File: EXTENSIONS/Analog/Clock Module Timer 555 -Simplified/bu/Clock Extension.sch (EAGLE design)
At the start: 8 parts, among them T555_CLOCK NE555N, X1 USB-A

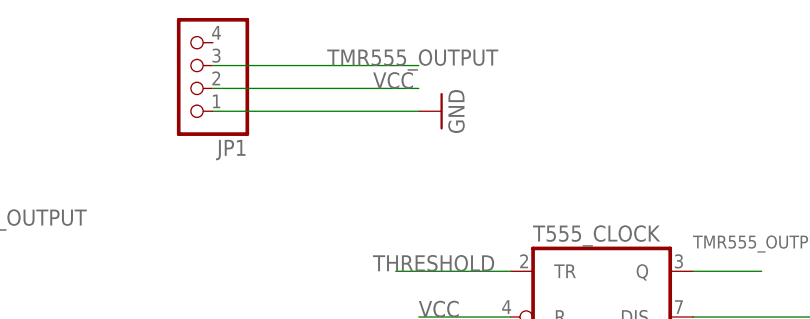
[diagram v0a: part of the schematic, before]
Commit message: fix bug in pcb '0 TO 9 Counter 74LS90'
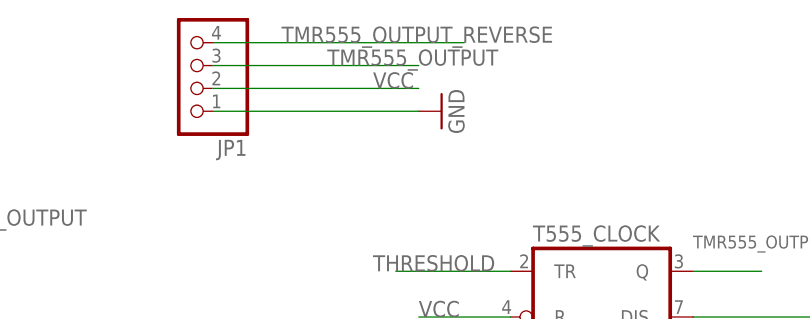
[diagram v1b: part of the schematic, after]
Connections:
- new net TMR555_OUTPUT_REVERSE: JP1.4
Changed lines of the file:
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@@
+</segment>
+</net>
+<net name="TMR555_OUTPUT_REVERSE" class="0">
+<segment>
+<pinref part="JP1" gate="A" pin="4"/>
+<wire x1="20.32" y1="129.54" x2="48.26" y2="129.54" width="0.1524" layer="91"/>
+<label x="27.94" y="129.54" size="1.778" layer="95"/>
 </segment>
 </net>
